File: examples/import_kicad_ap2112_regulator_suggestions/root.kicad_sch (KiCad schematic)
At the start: 2 parts, among them U1 GENERIC_MCU

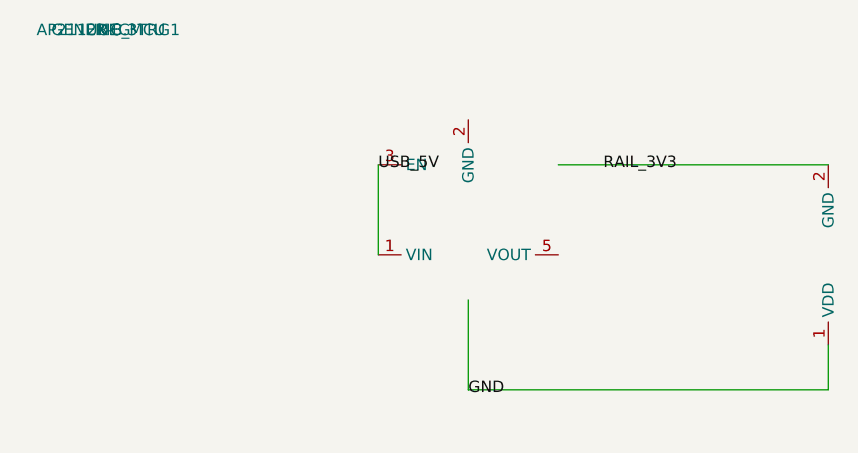
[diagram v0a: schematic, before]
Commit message: Validate AP2112 regulator support capacitors
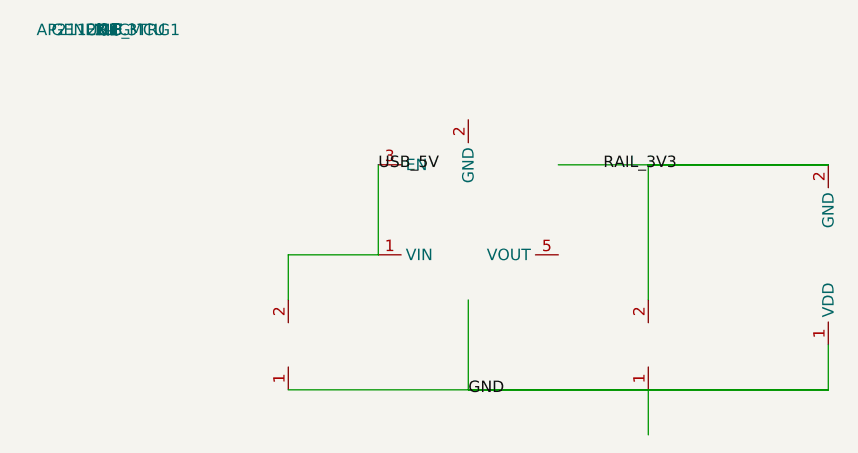
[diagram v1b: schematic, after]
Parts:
- added C1, C2: 1uF, symbol Device:C
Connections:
- net GND: now also C1.1
- net RAIL_3V3: now also C2.2
- net USB_5V: now also C1.2
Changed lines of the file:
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@@
     (property "Value" "GENERIC_MCU")
     (pin "1") (pin "2"))
-  (wire (pts (xy 30 15) (xy 30 25)))
+  (symbol (lib_id "Device:C") (at 20 35 0)
+    (property "Reference" "C1")
+    (property "Value" "1uF")
+    (pin "1") (pin "2"))
+  (symbol (lib_id "Device:C") (at 60 35 0)
+    (property "Reference" "C2")
+    (property "Value" "1uF")
+    (pin "1") (pin "2"))
+  (wire (pts (xy 30 15) (xy 30 25) (xy 20 25) (xy 20 30)))
   (label "USB_5V" (at 30 15 0))
-  (wire (pts (xy 50 15) (xy 80 15)))
+  (wire (pts (xy 50 15) (xy 80 15) (xy 60 15) (xy 60 30)))
   (label "RAIL_3V3" (at 55 15 0))
   (wire (pts (xy 40 30) (xy 40 40) (xy 80 40) (xy 80 35)))
+  (wire (pts (xy 20 40) (xy 80 40)))
+  (wire (pts (xy 60 40) (xy 60 45)))
   (label "GND" (at 40 40 0))
 )
